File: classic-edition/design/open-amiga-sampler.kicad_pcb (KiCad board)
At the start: 2 copper layers, 37 x 34 mm, 19 parts, among them J1 Left, J2 Right, J3 DB25_Male, U1 ADC0820CCN, U2 MCP6002-xP

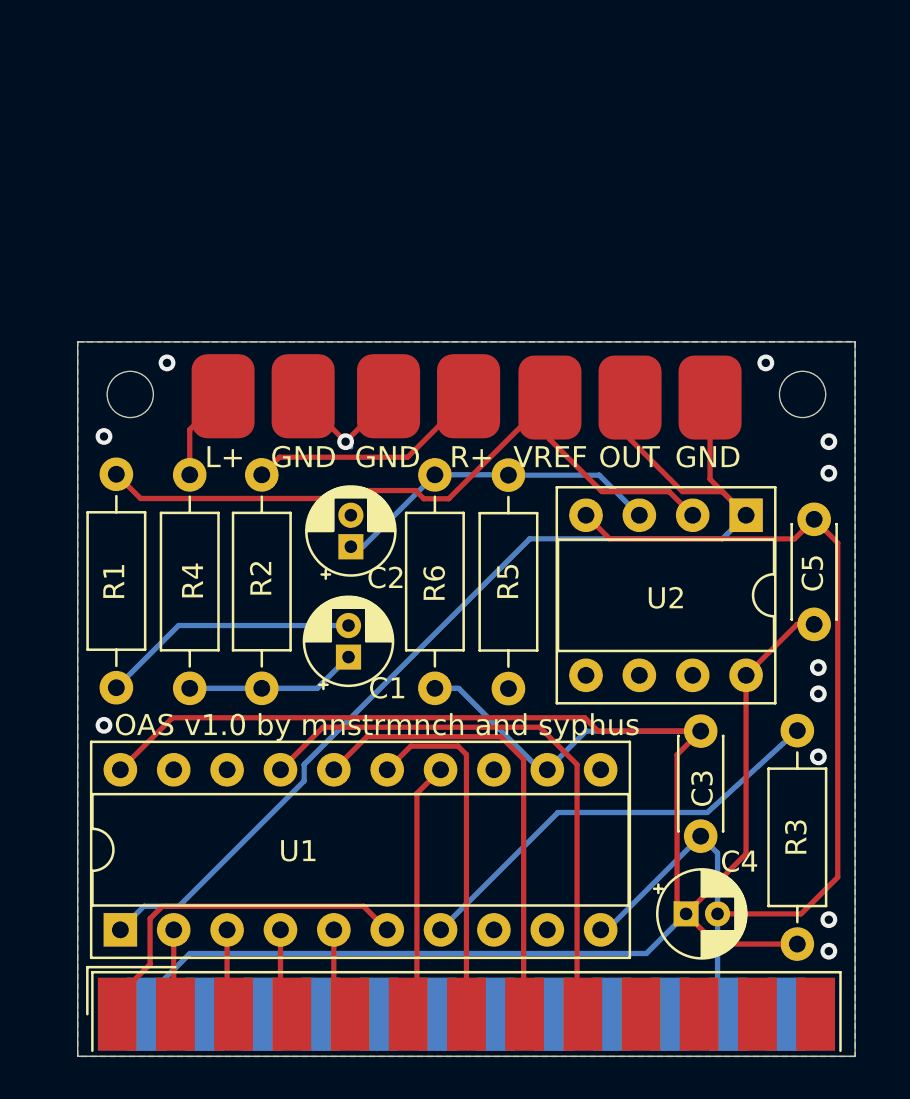
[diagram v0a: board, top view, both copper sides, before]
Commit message: major update to PCB
removed unnecessary traces and vias, re-routed everything, added footprints for gain pot and 3.5mm phone jack soldered direct to board
Lots of KiCad project cleanup: added netclasses, adjusted design rules, changed global labels to local (since the schematic only has one page) and unified the schematic so it is no longer in several separate pieces
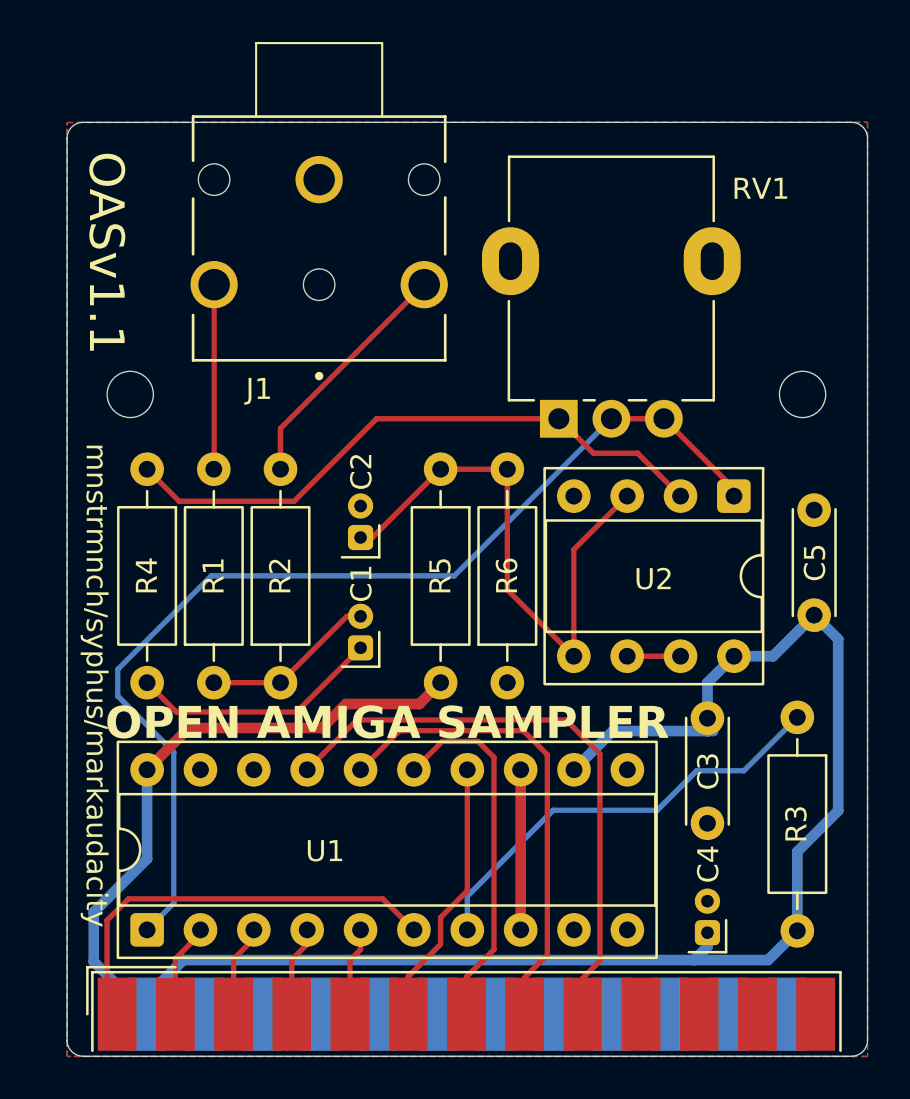
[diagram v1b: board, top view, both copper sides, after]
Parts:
- removed J2: Right, connectors:Audio pads
- C1: value 10uf -> 10uf tantalum^{:2}; moved to B.Cu
- C2, C3, C4, C5: moved to B.Cu
- J1: value Left -> 3.5mm stereo phone; footprint connectors:Audio pads -> Connector_Audio:Jack_3.5mm_CUI_SJ1-3543
- R5, R6: value 1K -> 100k^{:1}
- RV1: value R_POT -> 10k expo; footprint connectors:Pot pads -> Potentiometer_THT:Potentiometer_Alpha_RD901F-40-00D_Single_Vertical
- U2: value MCP6002-xP -> MCP6002-xP^{:3}
- moved J1 8.70 mm to (63.0, 20.3), turned to -90 degrees
- moved RV1 4.54 mm to (74.4, 31.7), turned to 90 degrees
- moved R4 1.48 mm to (54.8, 34.1)
- moved C4 1.36 mm to (81.5, 56.1), turned to 90 degrees
- moved U1 1.27 mm to (54.8, 56.0)
- moved R1 1.18 mm to (58.0, 44.2)
- moved U2 1.08 mm to (82.7, 35.3)
- moved R2 0.93 mm to (61.2, 44.2)
- moved C1 0.72 mm to (65.0, 42.6)
- moved C3 0.69 mm to (81.5, 45.9)
- moved C2 0.64 mm to (65.0, 37.3)
- moved R3 0.63 mm to (85.8, 45.9)
- moved C5 0.44 mm to (86.5, 41.0)
- moved R5 0.38 mm to (68.8, 34.1)
- moved R6 0.28 mm to (71.9, 44.2)
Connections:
- net D0 renamed /D0
- net D1 renamed /D1
- net D2 renamed /D2
- net D3 renamed /D3
- net D4 renamed /D4
- net D5 renamed /D5
- net D6 renamed /D6
- net D7 renamed /D7
- net STROBE renamed /STROBE
- net Vo renamed /AD_IN
- C1 pad 1: MONO_AUDIO -> Net-(C1-~-Pad1)
- C1 pad 2: Net-(C1-Pad2) -> Net-(C1-~-Pad2)
- C2 pad 1: Net-(C2-Pad1) -> Net-(U2A-+)
- J3 pad 10: Net-(J3-Pad10) -> unconnected-(J3-Pad10)
- J3 pad 11: Net-(J3-Pad11) -> unconnected-(J3-Pad11)
- J3 pad 12: Net-(J3-Pad12) -> unconnected-(J3-Pad12)
- J3 pad 13: Net-(J3-Pad13) -> unconnected-(J3-Pad13)
- J3 pad 15: Net-(J3-Pad15) -> unconnected-(J3-P15-Pad15)
- J3 pad 16: Net-(J3-Pad16) -> unconnected-(J3-P16-Pad16)
- J3 pad 17: Net-(J3-Pad17) -> unconnected-(J3-P17-Pad17)
- R1 pad 1: MONO_AUDIO -> Net-(C1-~-Pad2)
- R1 pad 2: Net-(J1-Pad1) -> Net-(J1-PadT)
- R2 pad 1: MONO_AUDIO -> Net-(C1-~-Pad2)
- R2 pad 2: Net-(J2-Pad1) -> Net-(J1-PadR)
- R4 pad 2: Net-(C1-Pad2) -> Net-(C1-~-Pad1)
- R5 pad 1: Net-(C2-Pad1) -> Net-(U2A-+)
- R6 pad 2: Net-(C2-Pad1) -> Net-(U2A-+)
- U1 pad 18: Net-(U1-Pad18) -> unconnected-(U1-~{OFL}-Pad18)
- U1 pad 9: Net-(U1-Pad9) -> unconnected-(U1-~{INT}-Pad9)
- U2 pad 3: Net-(C2-Pad1) -> Net-(U2A-+)
- U2 pad 5: (no net) -> Net-(U2A-+)
- U2 pad 6: (no net) -> Net-(U2B--)
- U2 pad 7: (no net) -> Net-(U2B--)
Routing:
- net GND: track 75.2 -> 7.67 mm, vias 12 -> 0
- net Net-(U2A-+): track 0.00 -> 27.2 mm
- net Net-(C2-Pad1): track 16.2 -> 0.00 mm
- net Net-(C1-Pad2): track 12.3 -> 0.00 mm
- net Net-(C1-~-Pad1): track 0.00 -> 12.0 mm
- net Net-(J1-PadR): track 0.00 -> 11.5 mm
- net Net-(J2-Pad1): track 11.4 -> 0.00 mm
- net Net-(J1-PadT): track 0.00 -> 8.47 mm
- net Net-(C1-~-Pad2): track 0.00 -> 8.29 mm
- net MONO_AUDIO: track 8.17 -> 0.00 mm
- net VCC: track 104.4 -> 96.6 mm
- net Net-(U2A--): track 33.7 -> 29.2 mm
- net Net-(J1-Pad1): track 4.40 -> 0.00 mm
- net /AD_IN: track 53.7 -> 50.0 mm
- net /STROBE: track 17.2 -> 20.3 mm
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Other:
- board size 37 x 34 mm -> 38.1 x 44.5 mm
- net class Default removed
- board text added: "C1"
- board text added: "C2"
- board text added: "C3"
- board text added: "C4"
- board text added: "C5"
- board text added: "OASv1.1"
- board text added: "OPEN AMIGA SAMPLER"
- board text added: "mnstrmnch/syphus/markaudacity"
- board text removed: "GND"
- board text removed: "L+"
- board text removed: "OAS v1.0 by mnstrmnch and syphus"
- board text removed: "OUT"
- board text removed: "R+"
- board text removed: "VREF"

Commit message: tweaks, edits, embedded models
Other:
- board text added: "ghOASt"
- board text added: "ghOASt v1.1"
- board text added: "github.com/markaudacity/ghOASt"
- board text added: "mnstrmnch/syphus/markaudacity 2020-2026"
- board text added: "v1.1"
- board text removed: "OASv1.1"
- board text removed: "mnstrmnch/syphus/markaudacity"

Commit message: fixing some sync oopsies
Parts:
- removed REF** (x2): MountingHole_2.2mm_M2, MountingHole:MountingHole_2.2mm_M2
- moved R4 109.2 mm to (146.2, 93.8), turned to 90 degrees
- moved R2 104.0 mm to (152.6, 93.8)
- moved R1 104.0 mm to (149.4, 93.8)
- moved J1 100.4 mm to (152.6, 65.5)
- moved R6 100.1 mm to (158.9, 93.8)
- moved R5 100.1 mm to (155.8, 83.6)
- moved R3 96.4 mm to (160.2, 107.1), turned to 90 degrees
- moved C1 93.6 mm to (147.0, 87.6), turned to -90 degrees
- moved C3 93.1 mm to (155.8, 102.0)
- moved J3 89.8 mm to (143.7, 111.4)
- moved U1 88.9 mm to (128.5, 105.8)
- moved C2 88.5 mm to (141.8, 81.3)
- moved C4 85.4 mm to (155.8, 98.2), turned to -90 degrees
- moved RV1 78.9 mm to (141.8, 72.8), turned to 180 degrees
- moved C5 74.0 mm to (141.8, 90.3), turned to 130 degrees
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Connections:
- RV1 pad : (no net) -> GND
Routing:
- net VCC: track 96.6 -> 56.7 mm
- net Net-(U2A--): track 29.2 -> 40.0 mm
- net Net-(U2A-+): track 27.2 -> 36.3 mm
- net Net-(C1-~-Pad1): track 12.0 -> 4.18 mm
- net /AD_IN: track 50.0 -> 42.2 mm
- net GND: track 7.67 -> 0.00 mm
- net Net-(J1-PadT): track 8.47 -> 13.7 mm
- net Net-(J1-PadR): track 11.5 -> 15.0 mm
- net Net-(U2B--): track 2.54 -> 0.00 mm
- net Net-(U1-MODE): track 20.8 -> 18.4 mm
- net /D6: track 22.9 -> 24.5 mm
- net /D4: track 12.8 -> 14.4 mm
- net /D0: track 4.51 -> 6.11 mm
- net /D2: track 4.32 -> 5.92 mm
- net /D3: track 4.22 -> 5.83 mm
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- added copper zone on B.Cu, net VCC
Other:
- board size 38.1 x 44.5 mm -> 38.1 x 50.8 mm
- board text added: "ghOASt v1.5"
- board text added: "v1.5"
- board text removed: "C2"
- board text removed: "ghOASt v1.1"
- board text removed: "v1.1"
